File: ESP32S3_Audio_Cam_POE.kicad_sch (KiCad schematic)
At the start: 485 parts, among them CN1 PJ-316C-6A, J1 Connector, USB-TYPE-C-16P, J10 Conn_01x02, J11 Conn_01x02, J12 Conn_01x02, J13 Conn_01x02, J14 Conn_01x02, J15 Conn_01x02, J16 Conn_01x02, J17 Conn_01x02, J18 Conn_01x02, J19 Conn_01x02, J2 Connector, USB-TYPE-C-16P, J3 Conn_01x02, J4 Conn_01x02, J5 Conn_01x03, J6 Conn_01x03, J7 Conn_01x03, J8 Conn_01x03, J9 HC-RJ45-055-4_8P8C_Shielded, Q1 AO3401A, Q2 AO3401A, Q3 AO3401A, Q4 AO3401A, Q5 AO3401A, Q6 AO3401A, Q7 AO3401A, Q8 AO3401A, T1 H1102NLT, U1 TLV62568DBVR, U10 W25Q128JVSIQ, U11 TM1637, U12 DS18B20U(UMW), U13 W25Q128JVSIQ, U14 DP9900M-5V, U15 MAX98357AETE+T, U16 ICS-43434, U17 ICS-43434, U18 AXP2101, U19 RFM69HCW, U2 MT9221CT-06BR5, U3 USBLC6-2SC6, U4 USBLC6-2SC6, U5 XC6206-1.5NR, U6 XC6206-2.8V, U7 ESP32-S3, U8 ESP32-S3, U9 W5500, X1 X322525MOB4SI, Y1 40MHz, 15pF, Y2 40MHz, 15pF, Y3 32.768KHz

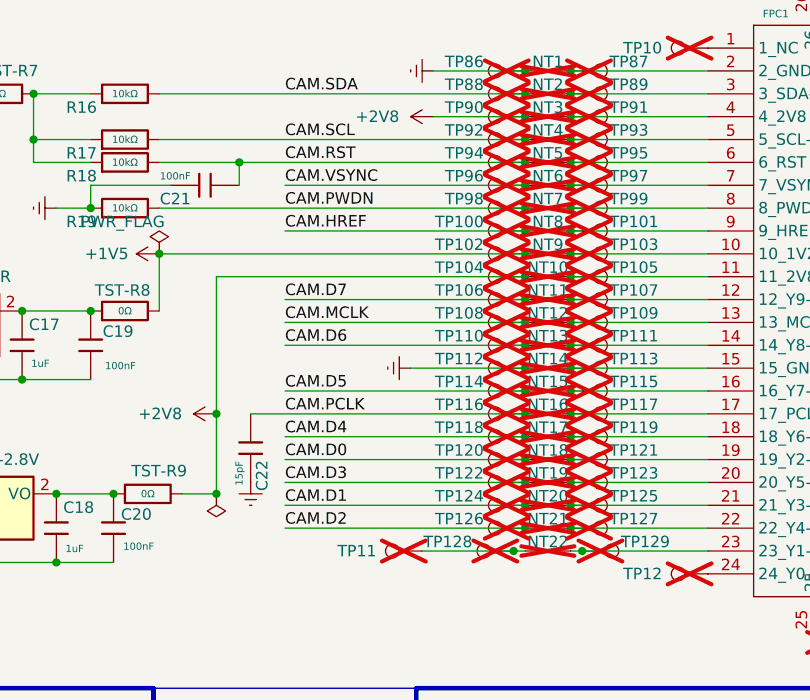
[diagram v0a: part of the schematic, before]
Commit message: Draft commit, added 33 ohms to camera lines to prevent cross talk
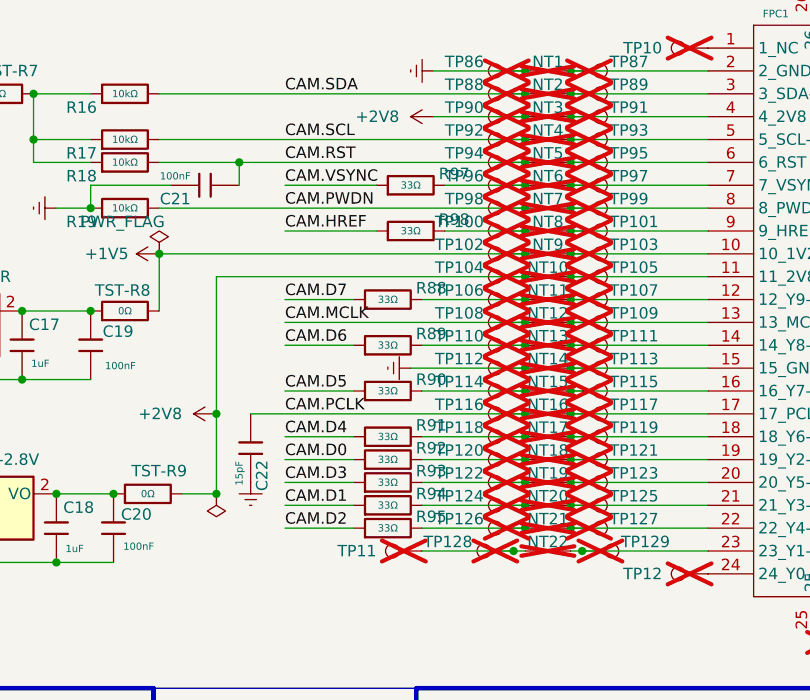
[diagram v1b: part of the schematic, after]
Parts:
- added R88, R89, R90, R91, R92, R93, R94, R95, R97, R98: 33Ω, PCM_JLCPCB:R_0402, symbol JLCPCB-Resistors:0402,33Ω
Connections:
- net CAM.D0: now also R92.1; no longer NT18.1, TP120.1
- net CAM.D1: now also R94.1; no longer NT20.1, TP124.1
- net CAM.D2: now also R95.1; no longer NT21.1, TP126.1
- net CAM.D3: now also R93.1; no longer NT19.1, TP122.1
- net CAM.D4: now also R91.1; no longer NT17.1, TP118.1
- net CAM.D5: now also R90.1; no longer NT15.1, TP114.1
- net CAM.D6: now also R89.1; no longer NT13.1, TP110.1
- net CAM.D7: now also R88.1; no longer NT11.1, TP106.1
- net CAM.HREF: now also R98.1; no longer NT8.1, TP100.1
- net CAM.VSYNC: now also R97.1; no longer NT6.1, TP96.1
- new net: NT13.1, R89.2, TP110.1
- new net: NT20.1, R94.2, TP124.1
- new net: NT17.1, R91.2, TP118.1
- new net: NT19.1, R93.2, TP122.1
- new net: NT21.1, R95.2, TP126.1
- new net: NT6.1, R97.2, TP96.1
- new net: NT8.1, R98.2, TP100.1
- new net: NT11.1, R88.2, TP106.1
- new net: NT15.1, R90.2, TP114.1
- new net: NT18.1, R92.2, TP120.1

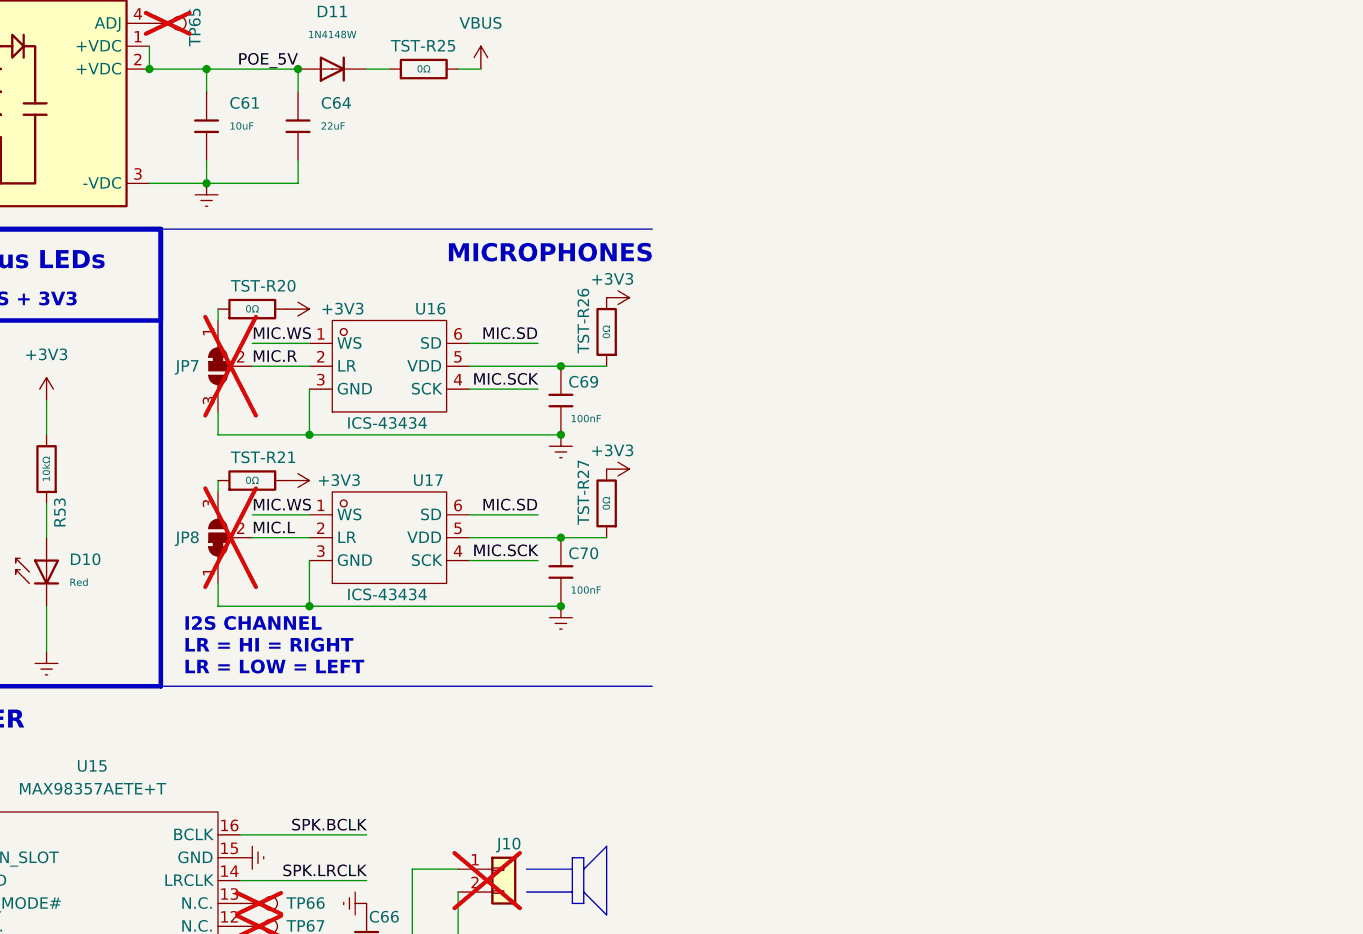
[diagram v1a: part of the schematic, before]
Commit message: updated to lower cost mic
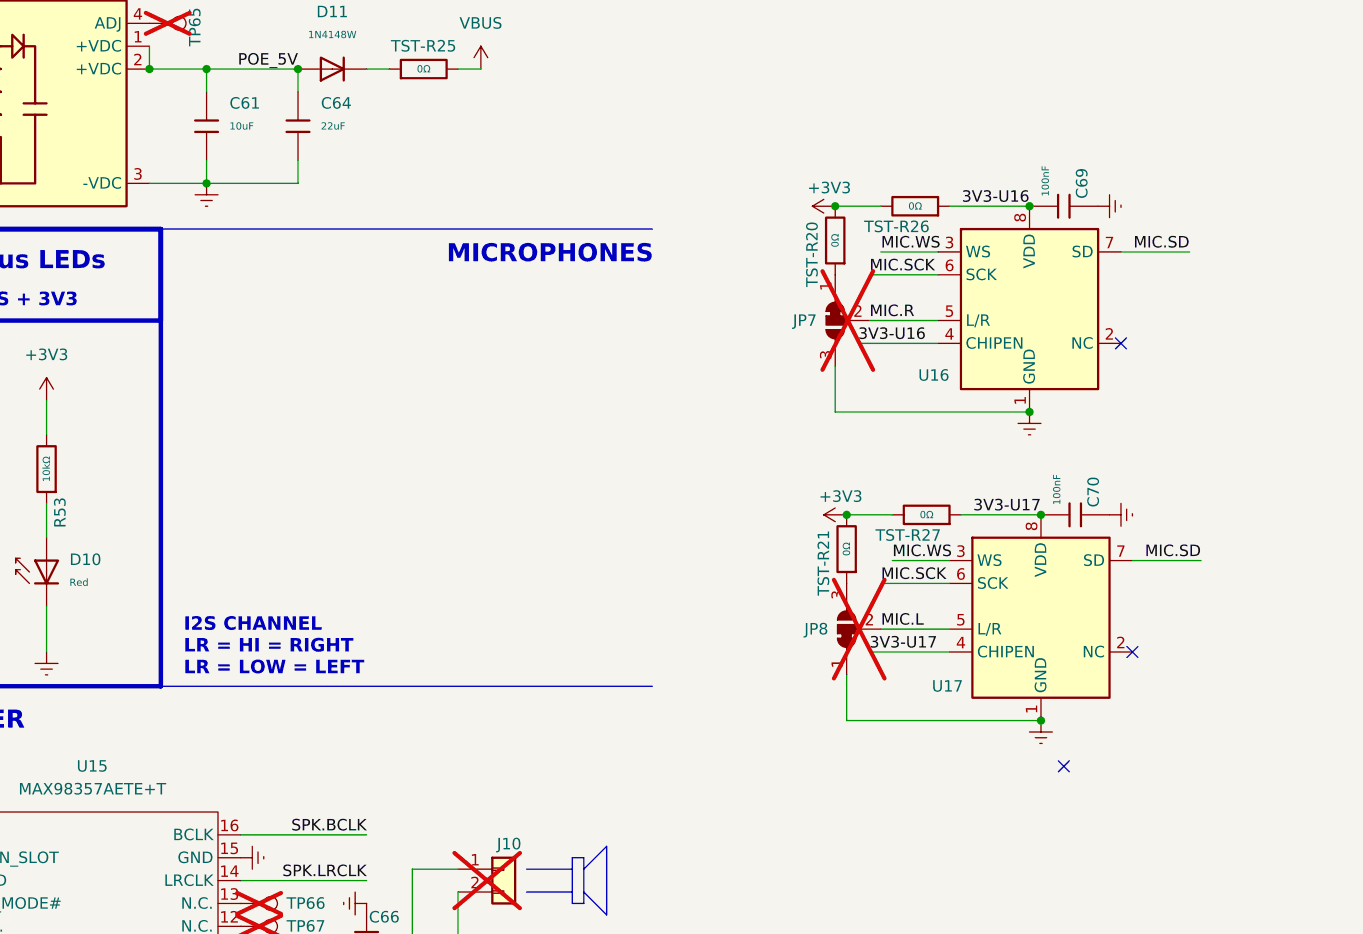
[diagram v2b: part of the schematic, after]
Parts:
- removed U16, U17: ICS-43434, JLCPCB:ICS-43434_C5656610, symbol JLCPCB-ICs:ICS-43434_C5656610
- added U16, U17: MSM261S4030H0R, Project-specific:LGA-8_4.0x3.0mm_P0.84mm_MSM261S4030H0R, symbol JLC_Convertered:MSM261S4030H0R
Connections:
- net COM: now also C69.2, C70.2, U16.1 (GND), U17.1 (GND); no longer C69.1, C70.1
- net MIC.L: now also U17.5 (L/R)
- net MIC.R: now also U16.5 (L/R)
- net MIC.SCK: now also U16.6 (SCK), U17.6 (SCK)
- net MIC.SD: now also U16.7 (SD), U17.7 (SD)
- net MIC.WS: now also U16.3 (WS), U17.3 (WS)
- net 3V3-U17: now reaches TST-R27.1
- net 3V3-U17: now also C70.1, U17.4 (CHIPEN), U17.8 (VDD); no longer C70.2
- net 3V3-U16: now reaches TST-R26.1
- net 3V3-U16: now also C69.1, U16.4 (CHIPEN), U16.8 (VDD); no longer C69.2
- no-connect marks 33 -> 36
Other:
- moved on the sheet: C69, JP7, TST-R20, TST-R26

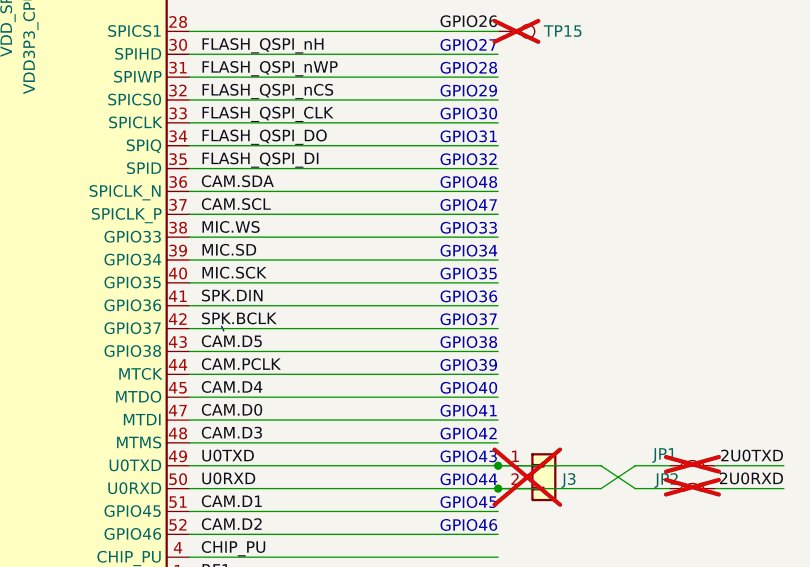
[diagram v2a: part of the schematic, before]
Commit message: added mic.sck, mic.sd, and mic.ws term resistors
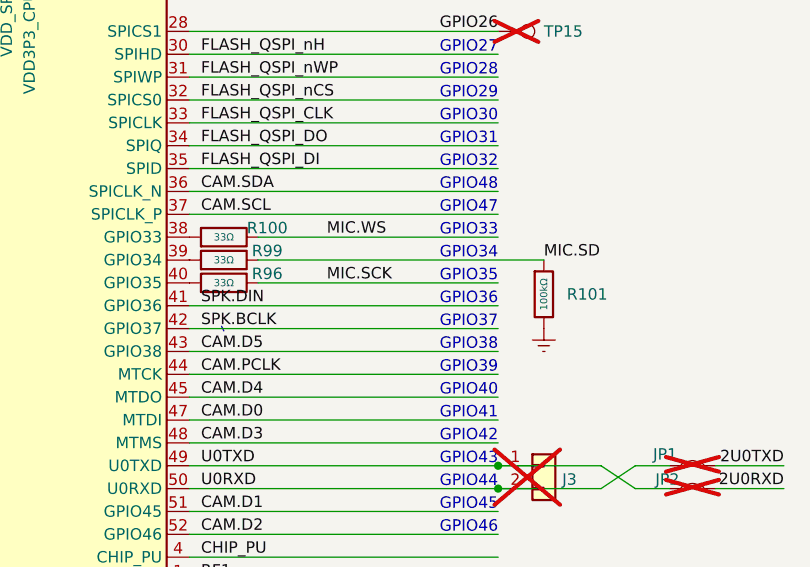
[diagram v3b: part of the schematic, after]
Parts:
- added R100, R96, R99: 33Ω, PCM_JLCPCB:R_0402, symbol JLCPCB-Resistors:0402,33Ω
- added R101: 100kΩ, PCM_JLCPCB:R_0402, symbol PCM_JLCPCB-Resistors:0402,100kΩ
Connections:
- net COM: now also R101.2
- net MIC.SCK: now also R96.2; no longer U7.40 (GPIO35)
- net MIC.SD: now also R101.1, R99.2; no longer U7.39 (GPIO34)
- net MIC.WS: now also R100.2; no longer U7.38 (GPIO33)
- new net: R99.1, U7.39 (GPIO34)
- new net: R100.1, U7.38 (GPIO33)
- new net: R96.1, U7.40 (GPIO35)

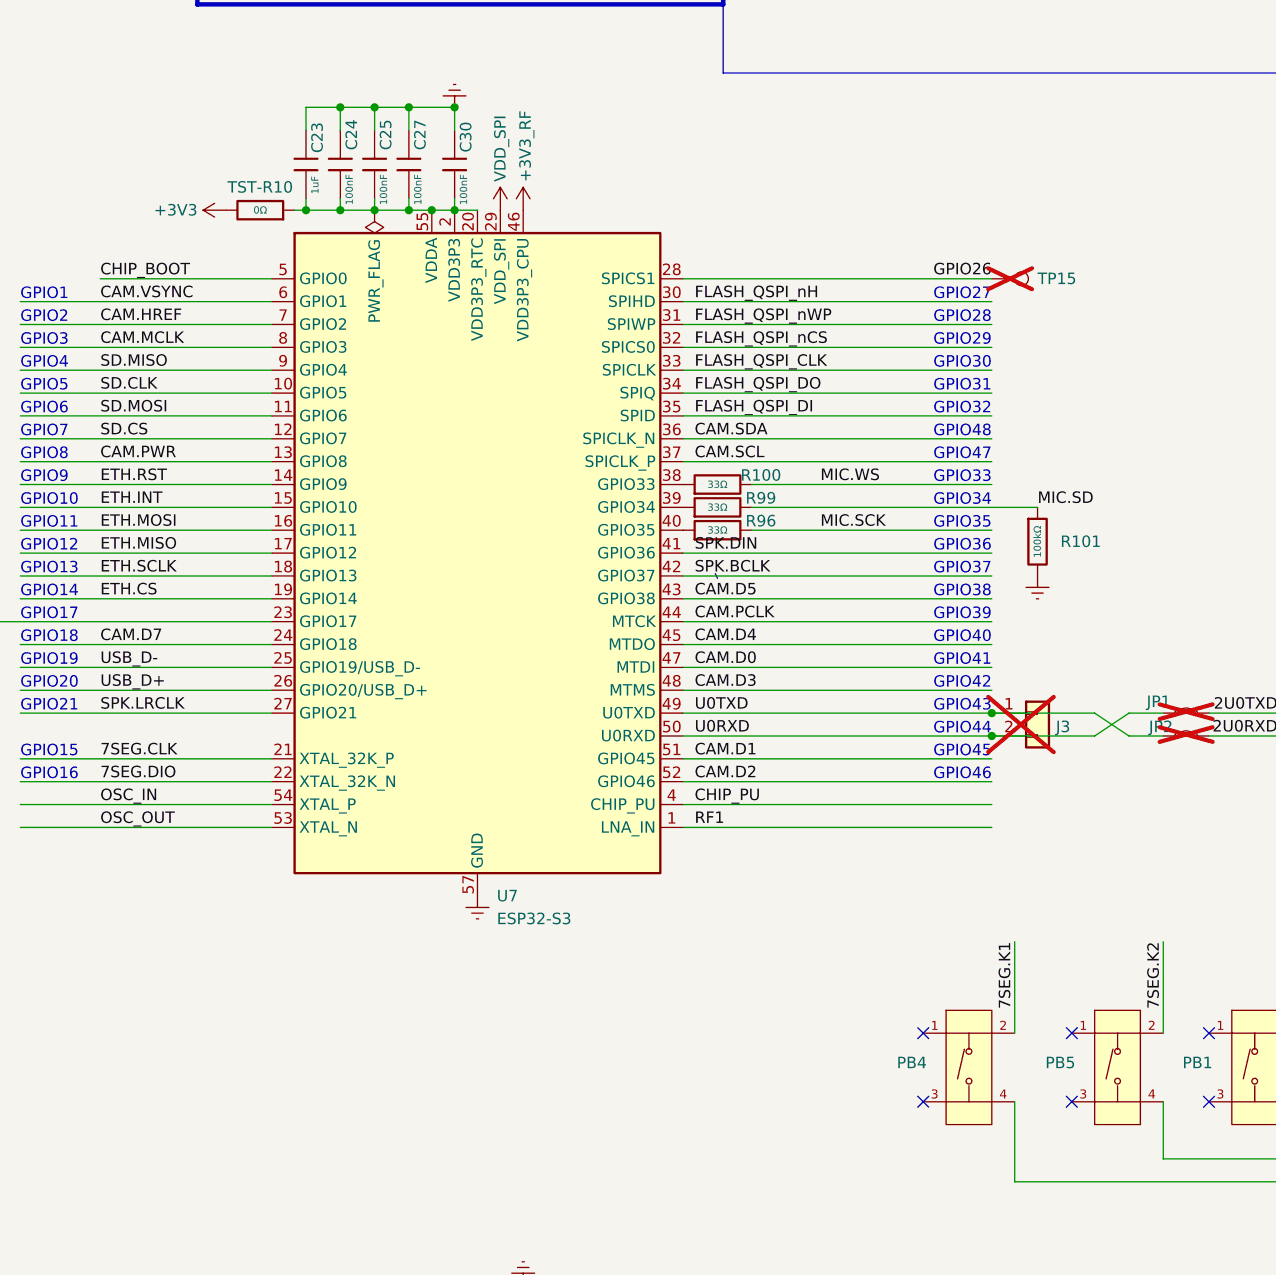
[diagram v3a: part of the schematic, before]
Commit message: moved nets off of conflicting psram IO.
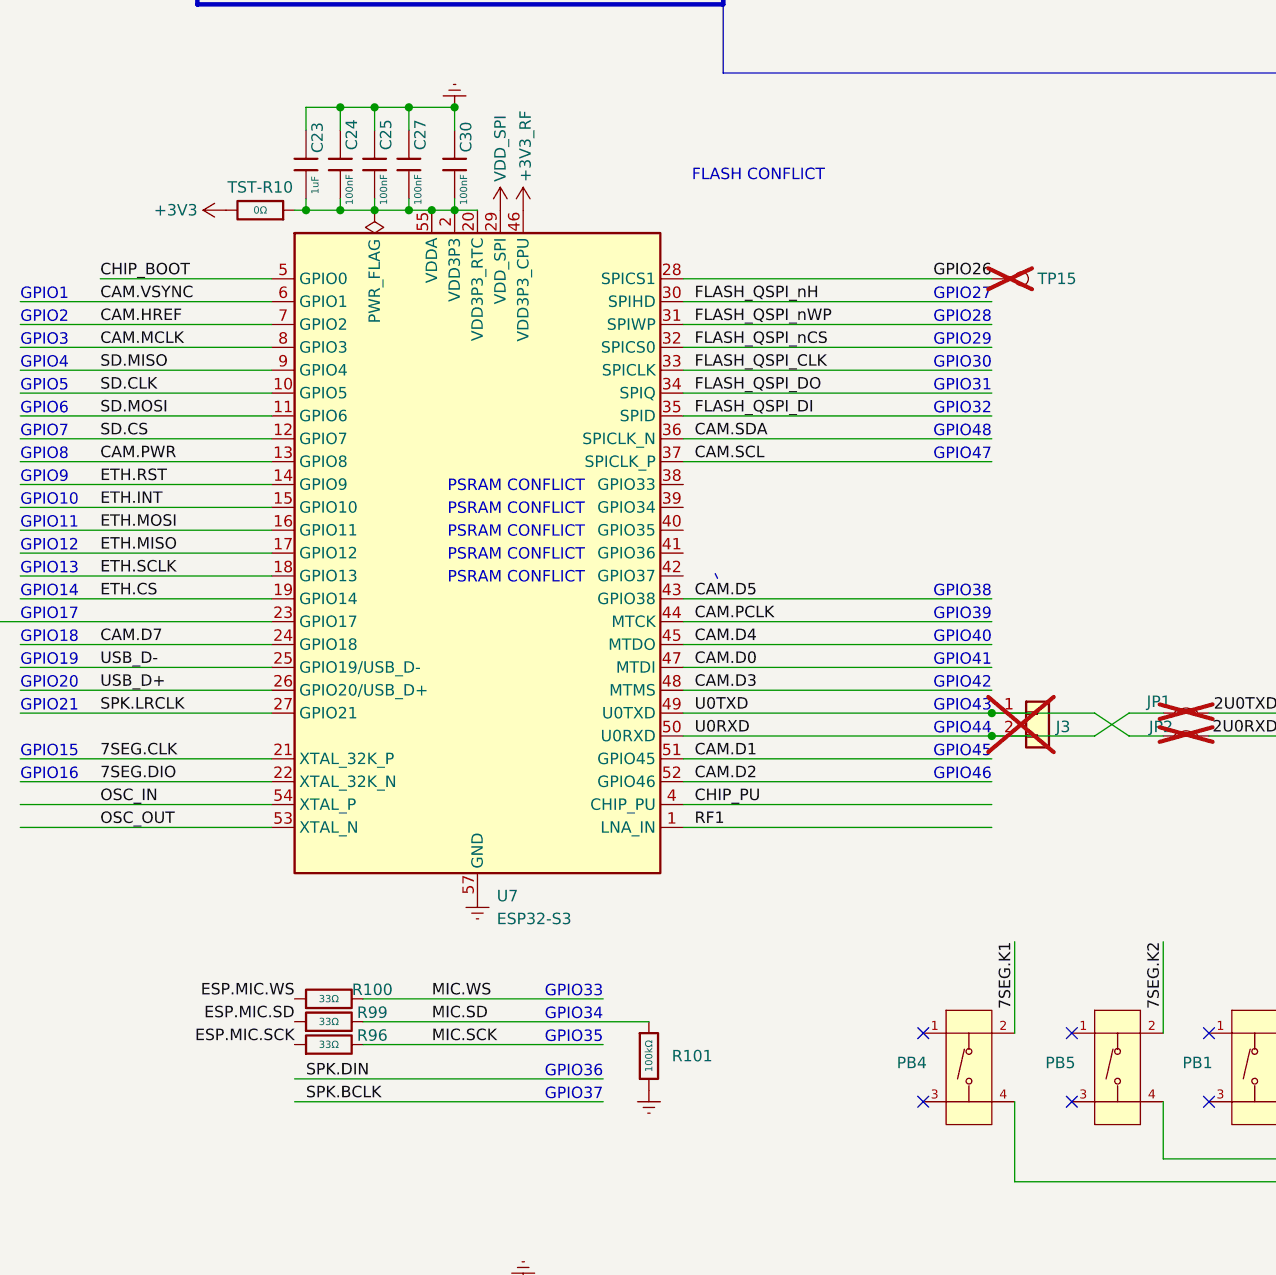
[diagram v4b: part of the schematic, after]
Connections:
- net SPK.BCLK: no longer U7.42 (GPIO37)
- net SPK.DIN: no longer U7.41 (GPIO36)
- net at U7.39 (GPIO34): no longer R99.1
- net at U7.38 (GPIO33): no longer R100.1
- net at U7.40 (GPIO35): no longer R96.1
- new net ESP.MIC.SCK: R96.1
- new net ESP.MIC.SD: R99.1
- new net ESP.MIC.WS: R100.1
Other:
- note added: "FLASH CONFLICT"
- note added: "PSRAM CONFLICT"
- moved on the sheet: R100, R101, R96, R99

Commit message: combined speaker and mic I2S signals making progress on IO count.
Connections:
- net ETH.MOSI is gone; now on net 7SEG.DIO: R25.1, U7.16 (GPIO11)
- net ETH.SCLK is gone; now on net 7SEG.CLK: R23.1, U7.18 (GPIO13)
- net SPK.BCLK is gone; now on net I2S.SCK: U15.16 (BCLK)
- net 7SEG.CLK: no longer U7.21 (XTAL_32K_P)
- net 7SEG.DIO: no longer U7.22 (XTAL_32K_N)
- net SPK.DIN: now also U7.27 (GPIO21)
- net MIC.SCK renamed I2S.SCK
- net MIC.WS renamed I2S.WS
- net I2S.WS: now also U15.14 (LRCLK)
- removed net SPK.LRCLK: U15.14 (LRCLK), U7.27 (GPIO21)
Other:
- note added: "SD IN 1 BIT MODE"
- note removed: "GPIO37"
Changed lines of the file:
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@@
 		)
 	)
-	(text "GPIO37"
-		(exclude_from_sim no)
-		(at 238.76 233.68 0)
-		(effects
-			(font
-				(size 1.27 1.27)
-			)
-			(justify right bottom)
-		)
-	)
 	(text "2GPIO21"
 		(exclude_from_sim no)
@@
 		)
 	)
+	(text "SD IN 1 BIT MODE"
+		(exclude_from_sim no)
+		(at 228.854 157.226 0)
+		(effects
+			(font
+				(size 1.27 1.27)
+			)
+			(justify right bottom)
+		)
+	)
 	(text "GPIO35"
 		(exclude_from_sim no)
@@
 	(wire
 		(pts
-			(xy 204.47 233.68) (xy 238.76 233.68)
-		)
-		(stroke
-			(width 0)
-			(type default)
-		)
-	)
-	(wire
-		(pts
 			(xy 327.66 149.86) (xy 327.66 152.4)
 		)
@@
 		)
 	)
-	(label "SPK.LRCLK"
-		(at 182.88 190.5 0)
-		(effects
-			(font
-				(size 1.27 1.27)
-			)
-			(justify left bottom)
-		)
-	)
 	(label "PMU.Vd2"
 		(at 214.63 387.35 180)
@@
 	)
 	(label "7SEG.CLK"
-		(at 182.88 195.58 0)
+		(at 193.04 175.26 0)
 		(effects
 			(font
@@
 		)
 	)
-	(label "MIC.SCK"
+	(label "I2S.SCK"
 		(at 571.5 158.75 0)
 		(effects
@@
 		)
 	)
-	(label "MIC.WS"
+	(label "I2S.WS"
 		(at 571.5 121.92 0)
 		(effects
@@
 	)
 	(label "7SEG.DIO"
-		(at 182.88 198.12 0)
+		(at 193.04 170.18 0)
 		(effects
 			(font
@@
 		)
 	)
-	(label "MIC.SCK"
+	(label "I2S.SCK"
 		(at 219.71 227.33 0)
 		(effects
@@
 		)
 	)
-	(label "SPK.BCLK"
+	(label "I2S.SCK"
 		(at 514.35 186.69 180)
 		(effects
@@
 	)
 	(label "SPK.DIN"
-		(at 205.74 231.14 0)
+		(at 182.88 190.5 0)
 		(effects
 			(font
@@
 		)
 	)
-	(label "MIC.WS"
+	(label "I2S.WS"
 		(at 572.77 156.21 0)
 		(effects
@@
 		)
 	)
-	(label "MIC.WS"
+	(label "I2S.WS"
 		(at 219.71 222.25 0)
 		(effects
@@
 		)
 	)
-	(label "MIC.SCK"
+	(label "I2S.SCK"
 		(at 570.23 124.46 0)
 		(effects
@@
 		)
 	)
-	(label "SPK.LRCLK"
+	(label "I2S.WS"
 		(at 514.35 191.77 180)
 		(effects
@@
 		)
 	)
-	(label "SPK.BCLK"
-		(at 205.74 233.68 0)
-		(effects
-			(font
-				(size 1.27 1.27)
-			)
-			(justify left bottom)
-		)
-	)
